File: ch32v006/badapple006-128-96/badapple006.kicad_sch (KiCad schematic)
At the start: 28 parts, among them J10 OLEDGPIO, J11 PGM, J2 USB_C_Receptacle_USB2.0, J6 RFO, J7 RFA, J8 APPLE, J9 RB132-2896GSWHG_01, U1 CH32V006F8U6, U2 XC6206P332, Y1 24MHz

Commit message: General updates for order
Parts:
- added C14, C15: 2.2u16v, Capacitor_SMD:C_0402_1005Metric, symbol Device:C
- J10, J2, J6, J7, J8: now not fitted; now left out of the parts list
- R1: value 390k -> 1M; LCSC C25782 -> C26083
- U1: LCSC (none) -> C42431288
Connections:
- net GND: now also C14.2, C15.2
- net OVDD: no longer J9.6 (Pin_6)
- net VCOMH: now also C15.1
- new net OVDDB: C14.1, J9.6 (Pin_6)

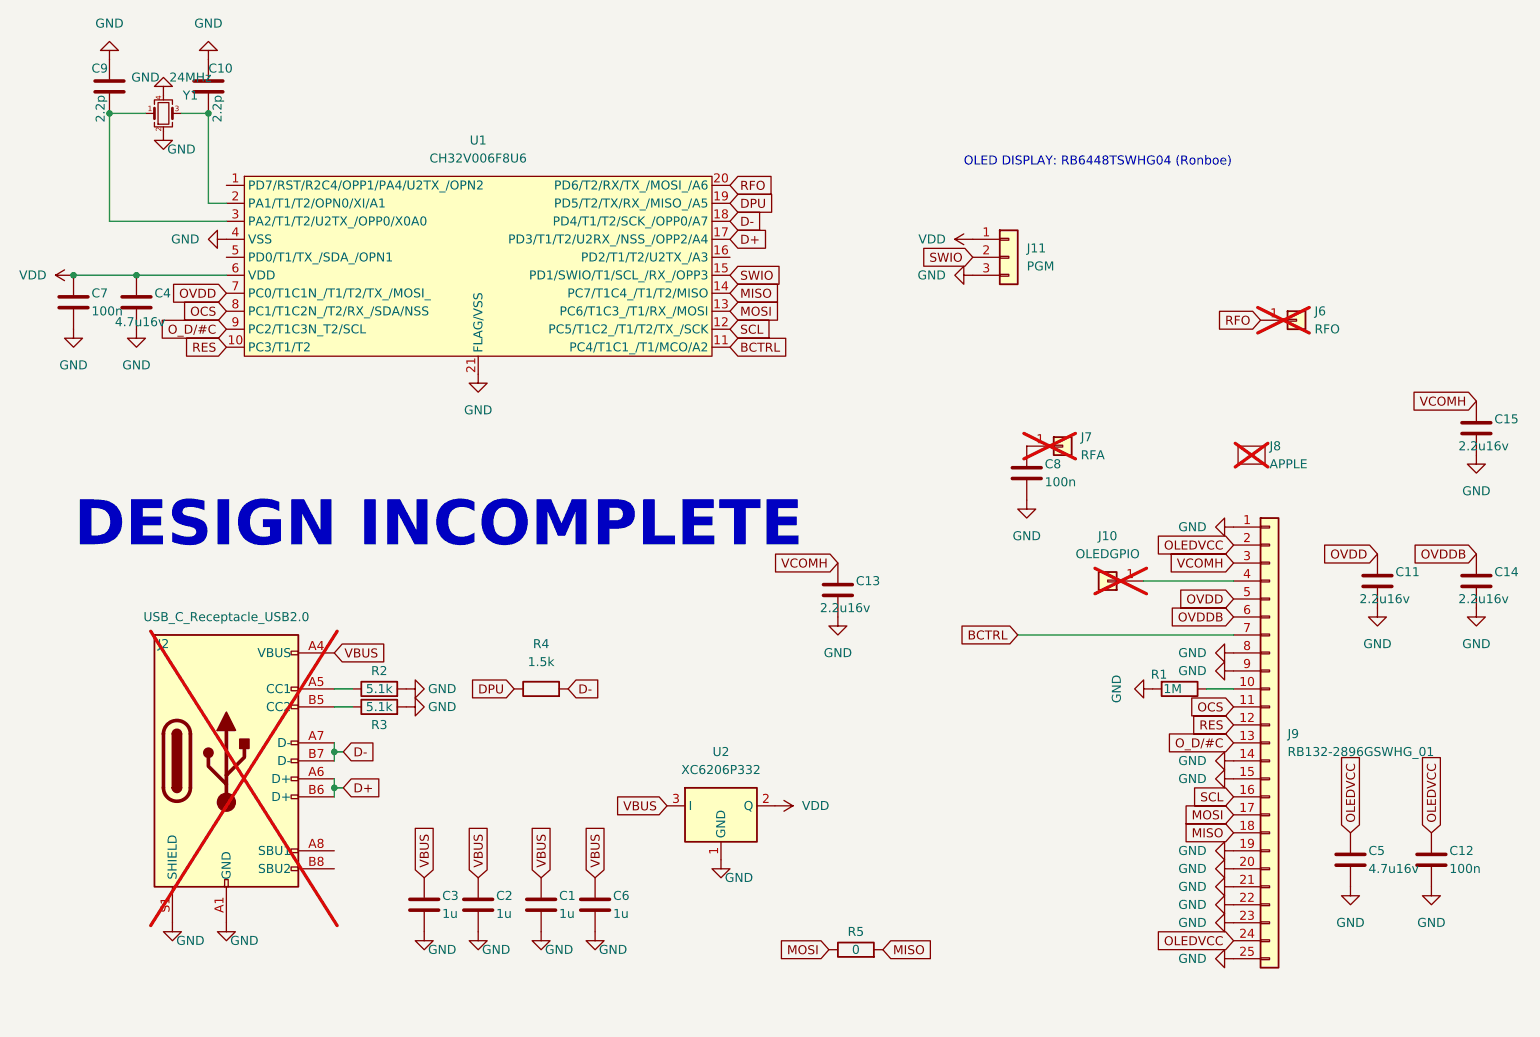
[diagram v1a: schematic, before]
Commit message: Update 006 board + add boost supply.
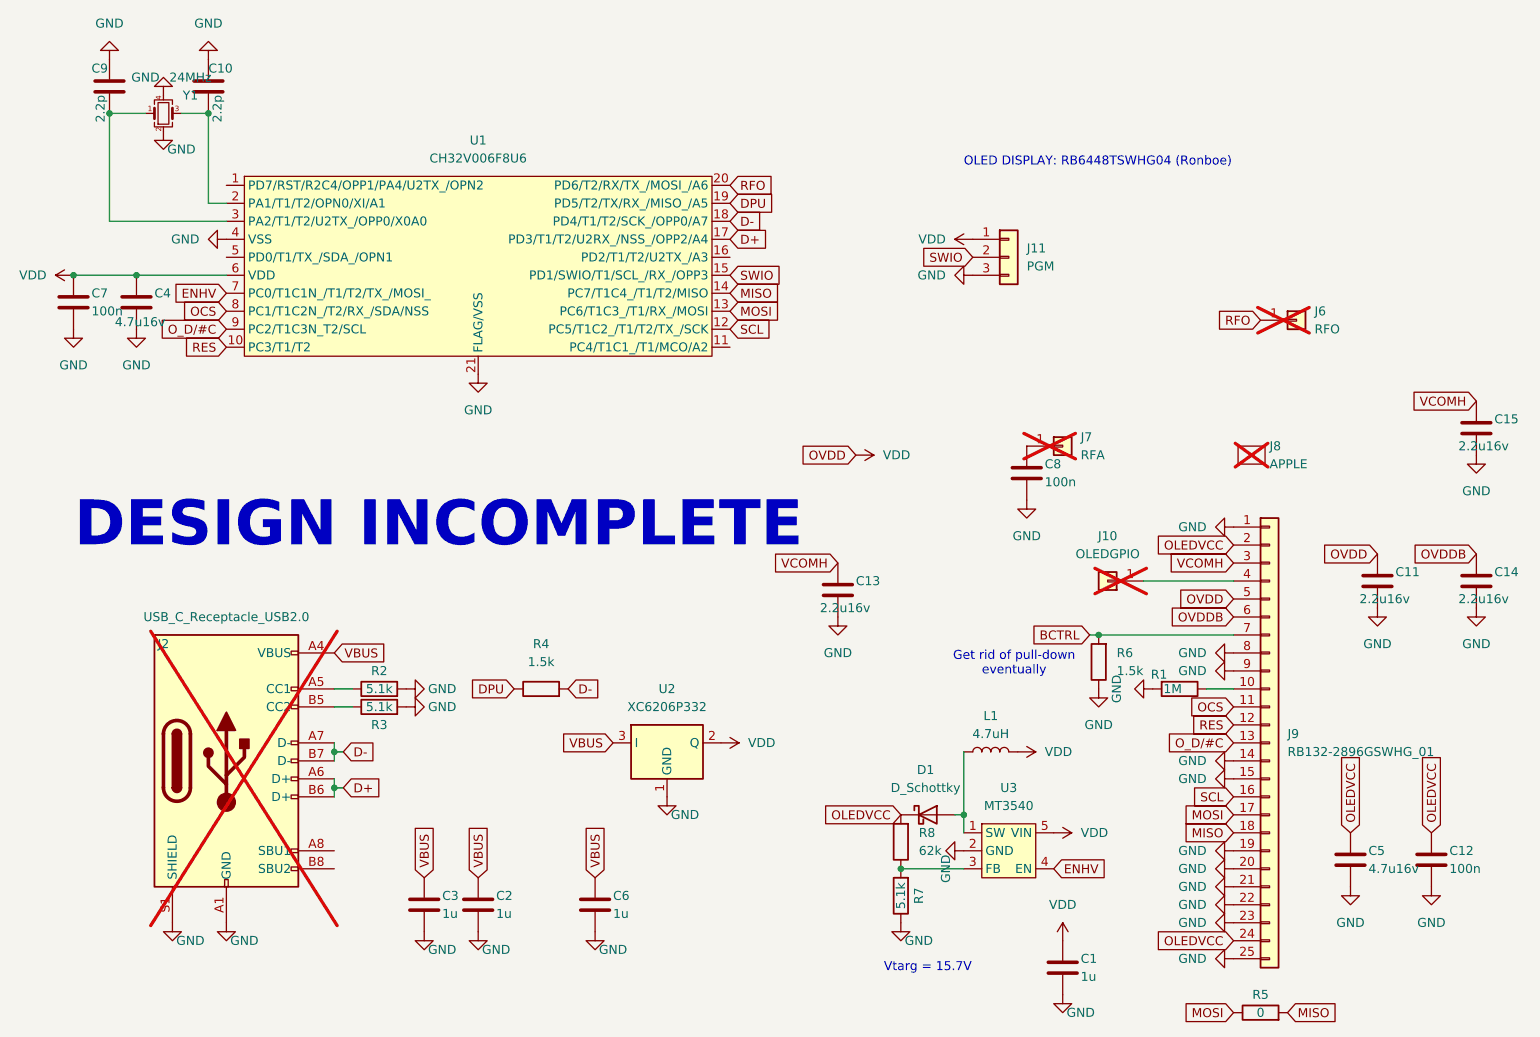
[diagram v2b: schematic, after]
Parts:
- added D1: D_Schottky, Diode_SMD:D_SOD-323, symbol Device:D_Schottky
- added L1: 4.7uH, Inductor_SMD:L_0603_1608Metric, symbol Device:L
- added R6: 1.5k, Resistor_SMD:R_0402_1005Metric, symbol Device:R
- added R7: 5.1k, Resistor_SMD:R_0402_1005Metric, symbol Device:R
- added R8: 62k, Resistor_SMD:R_0402_1005Metric, symbol Device:R
- added U3: MT3540, Package_TO_SOT_SMD:SOT-23-5, symbol cnhardware:MT3540
- Y1: LCSC C2929397 -> C20623621
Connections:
- net BCTRL: now also R6.2; no longer U1.11 (PC4/T1C1_/T1/MCO/A2)
- net GND: now also R6.1, R7.1, U3.2 (GND)
- net OLEDVCC: now also D1.1 (K), R8.2
- net VBUS: no longer C1.1
- net VDD: now also C1.1, C11.1, J9.5 (Pin_5), L1.2, U3.5 (VIN)
- removed net OVDD: C11.1, J9.5 (Pin_5), U1.7 (PC0/T1C1N_/T1/T2/TX_/MOSI_)
- new net: D1.2 (A), L1.1, U3.1 (SW)
- new net: R7.2, R8.1, U3.3 (FB)
- new net ENHV: U1.7 (PC0/T1C1N_/T1/T2/TX_/MOSI_), U3.4 (EN)
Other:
- note added: "Get rid of pull-down eventually"
- note added: "Vtarg = 15.7V"
- moved on the sheet: R5, U2
